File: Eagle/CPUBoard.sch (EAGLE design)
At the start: 32 parts, among them IC2 MAX232, IC3 MAX485CPA, J1 DISPLAY, J2 BUTTON_BOARD, J3 RELAY_BOARD, Q1 12.000MHz, X6 MKDSN1,5/3-5,08, X7 MKDSN1,5/3-5,08

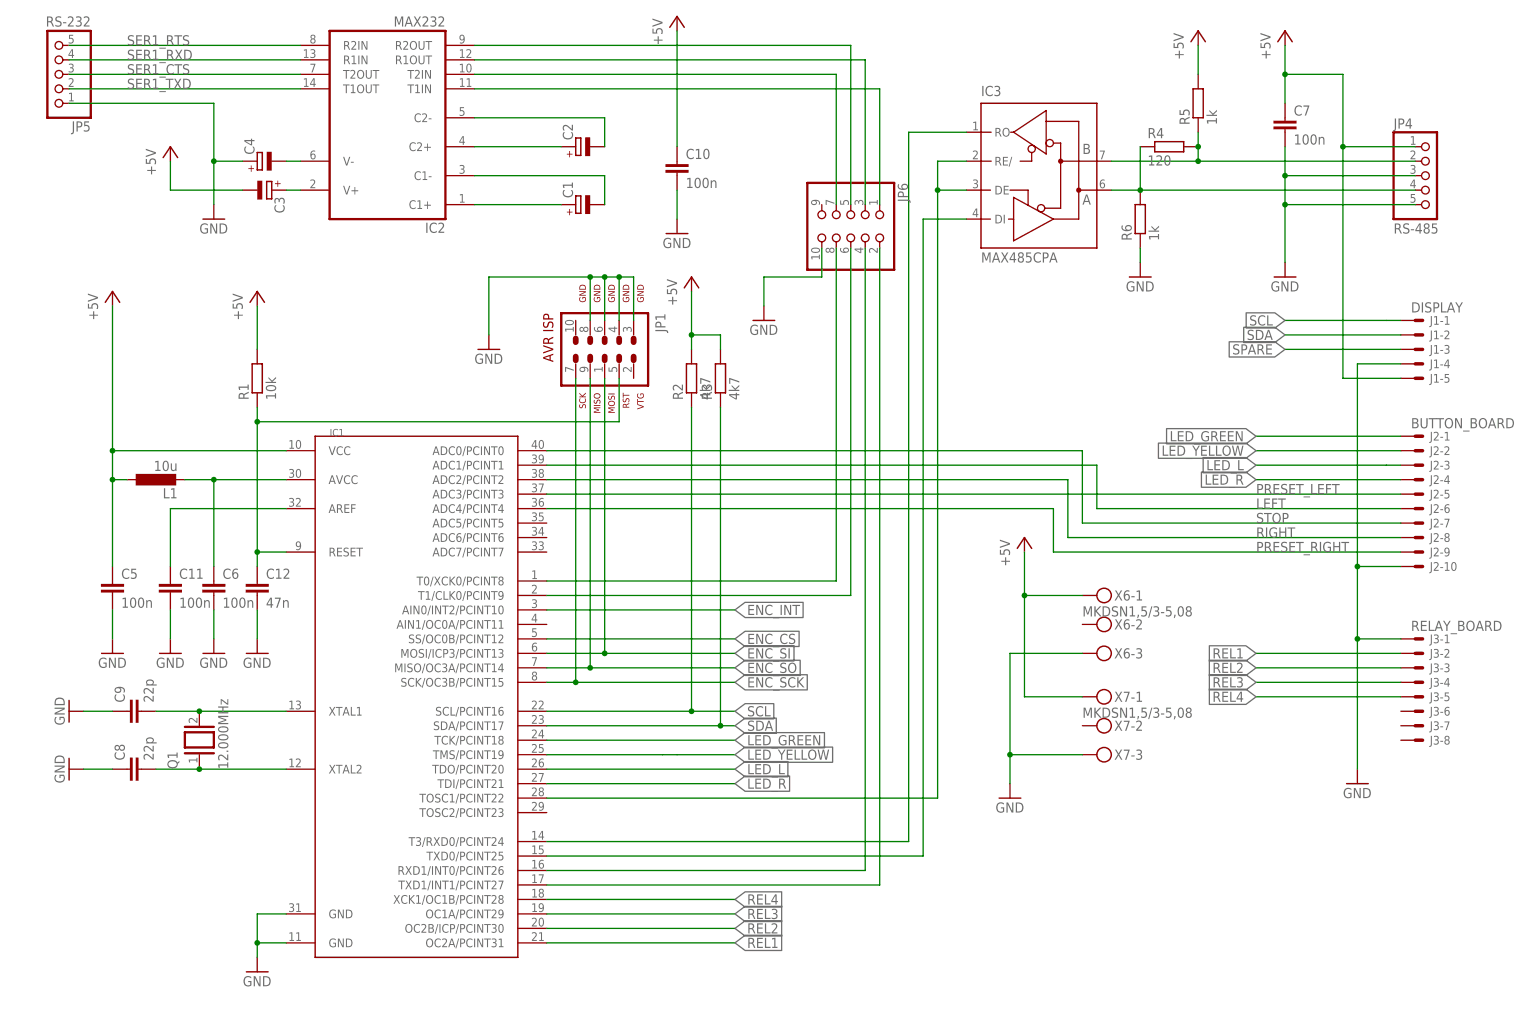
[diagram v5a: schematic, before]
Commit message: - corrections for RelayBoard1:   - using right connectors from library con-molex   - single sided routing - corrections for ButtonBoard:   - using right connector from library con-molex   - using right switches from library switch-misc (SRK/SRKL) - component placement & board layout for ButtonBoard done - CPUBoard:   - some components moved around the board   - re-routing (partially)
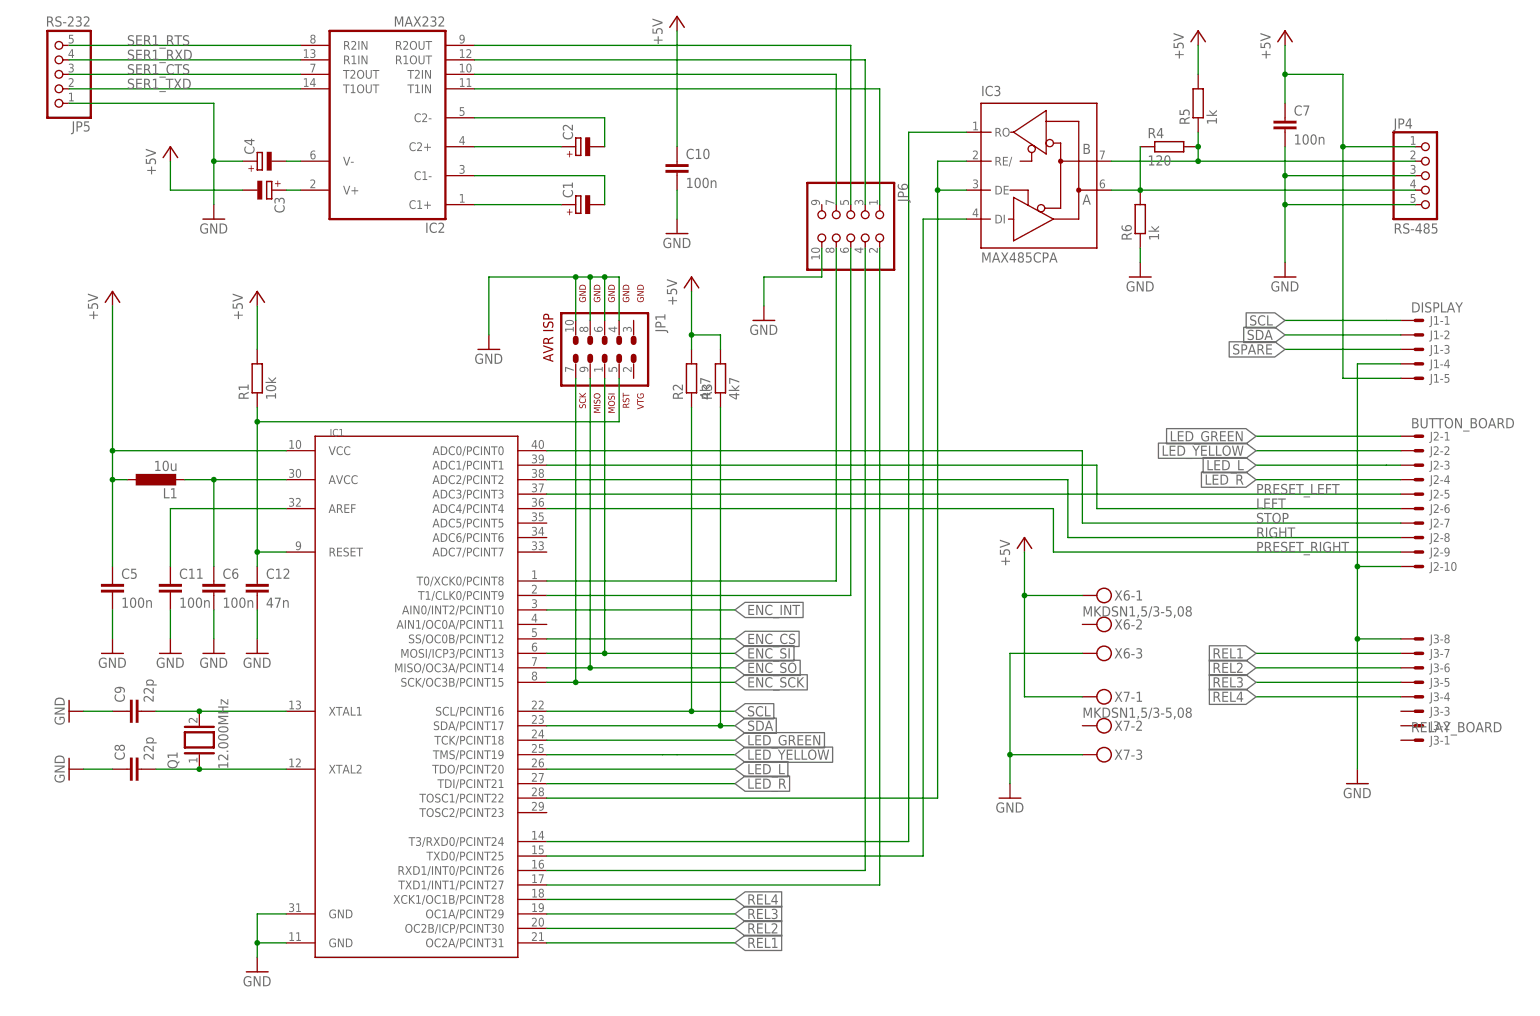
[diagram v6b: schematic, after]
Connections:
- net GND: now also J3-8.S, JP1.10; no longer J3-1.S, JP1.3
- net REL1: now also J3-7.S; no longer J3-2.S
- net REL2: now also J3-6.S; no longer J3-3.S
- net REL3: now also J3-5.S; no longer J3-4.S
- net REL4: now also J3-4.S; no longer J3-5.S
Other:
- moved on the sheet: J3-1, J3-2, J3-3, J3-4, J3-5, J3-6, J3-7, J3-8
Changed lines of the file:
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@@
 <instance part="J2" gate="-9" x="243.84" y="83.82"/>
 <instance part="J2" gate="-10" x="243.84" y="81.28"/>
-<instance part="J3" gate="-1" x="243.84" y="68.58"/>
-<instance part="J3" gate="-2" x="243.84" y="66.04"/>
-<instance part="J3" gate="-3" x="243.84" y="63.5"/>
-<instance part="J3" gate="-4" x="243.84" y="60.96"/>
-<instance part="J3" gate="-5" x="243.84" y="58.42"/>
-<instance part="J3" gate="-6" x="243.84" y="55.88"/>
-<instance part="J3" gate="-7" x="243.84" y="53.34"/>
-<instance part="J3" gate="-8" x="243.84" y="50.8"/>
+<instance part="J3" gate="-1" x="243.84" y="50.8"/>
+<instance part="J3" gate="-2" x="243.84" y="53.34"/>
+<instance part="J3" gate="-3" x="243.84" y="55.88"/>
+<instance part="J3" gate="-4" x="243.84" y="58.42"/>
+<instance part="J3" gate="-5" x="243.84" y="60.96"/>
+<instance part="J3" gate="-6" x="243.84" y="63.5"/>
+<instance part="J3" gate="-7" x="243.84" y="66.04"/>
+<instance part="J3" gate="-8" x="243.84" y="68.58"/>
 </instances>
 <busses>
@@
 </segment>
 <segment>
-<pinref part="JP1" gate="G$1" pin="3"/>
-<wire x1="106.68" y1="124.46" x2="106.68" y2="132.08" width="0.1524" layer="91"/>
-<wire x1="106.68" y1="132.08" x2="104.14" y2="132.08" width="0.1524" layer="91"/>
 <pinref part="GND10" gate="1" pin="GND"/>
 <wire x1="104.14" y1="132.08" x2="101.6" y2="132.08" width="0.1524" layer="91"/>
 <wire x1="101.6" y1="132.08" x2="99.06" y2="132.08" width="0.1524" layer="91"/>
-<wire x1="99.06" y1="132.08" x2="81.28" y2="132.08" width="0.1524" layer="91"/>
+<wire x1="99.06" y1="132.08" x2="96.52" y2="132.08" width="0.1524" layer="91"/>
+<wire x1="96.52" y1="132.08" x2="81.28" y2="132.08" width="0.1524" layer="91"/>
 <wire x1="81.28" y1="132.08" x2="81.28" y2="121.92" width="0.1524" layer="91"/>
 <pinref part="JP1" gate="G$1" pin="4"/>
 <wire x1="104.14" y1="124.46" x2="104.14" y2="132.08" width="0.1524" layer="91"/>
-<junction x="104.14" y="132.08"/>
 <pinref part="JP1" gate="G$1" pin="6"/>
 <wire x1="101.6" y1="124.46" x2="101.6" y2="132.08" width="0.1524" layer="91"/>
@@
 <wire x1="99.06" y1="124.46" x2="99.06" y2="132.08" width="0.1524" layer="91"/>
 <junction x="99.06" y="132.08"/>
+<pinref part="JP1" gate="G$1" pin="10"/>
+<wire x1="96.52" y1="124.46" x2="96.52" y2="132.08" width="0.1524" layer="91"/>
+<junction x="96.52" y="132.08"/>
 </segment>
 <segment>
 <pinref part="GND11" gate="1" pin="GND"/>
 <wire x1="233.68" y1="45.72" x2="233.68" y2="68.58" width="0.1524" layer="91"/>
-<wire x1="233.68" y1="68.58" x2="241.3" y2="68.58" width="0.1524" layer="91"/>
+<wire x1="233.68" y1="68.58" x2="233.68" y2="81.28" width="0.1524" layer="91"/>
 <wire x1="241.3" y1="81.28" x2="233.68" y2="81.28" width="0.1524" layer="91"/>
-<wire x1="233.68" y1="81.28" x2="233.68" y2="68.58" width="0.1524" layer="91"/>
-<junction x="233.68" y="68.58"/>
 <wire x1="233.68" y1="116.84" x2="233.68" y2="81.28" width="0.1524" layer="91"/>
 <junction x="233.68" y="81.28"/>
@@
 <pinref part="J1" gate="-4" pin="S"/>
 <pinref part="J2" gate="-10" pin="S"/>
-<pinref part="J3" gate="-1" pin="S"/>
+<pinref part="J3" gate="-8" pin="S"/>
+<wire x1="241.3" y1="68.58" x2="233.68" y2="68.58" width="0.1524" layer="91"/>
+<junction x="233.68" y="68.58"/>
 </segment>
 <segment>
@@
 <net name="REL1" class="0">
 <segment>
-<wire x1="241.3" y1="66.04" x2="215.9" y2="66.04" width="0.1524" layer="91"/>
 <label x="215.9" y="66.04" size="1.778" layer="95" rot="MR0" xref="yes"/>
-<pinref part="J3" gate="-2" pin="S"/>
+<pinref part="J3" gate="-7" pin="S"/>
+<wire x1="215.9" y1="66.04" x2="241.3" y2="66.04" width="0.1524" layer="91"/>
 </segment>
 <segment>
@@
 <net name="REL2" class="0">
 <segment>
+<label x="215.9" y="63.5" size="1.778" layer="95" rot="MR0" xref="yes"/>
+<pinref part="J3" gate="-6" pin="S"/>
 <wire x1="241.3" y1="63.5" x2="215.9" y2="63.5" width="0.1524" layer="91"/>
-<label x="215.9" y="63.5" size="1.778" layer="95" rot="MR0" xref="yes"/>
-<pinref part="J3" gate="-3" pin="S"/>
 </segment>
 <segment>
@@
 <net name="REL3" class="0">
 <segment>
-<wire x1="241.3" y1="60.96" x2="215.9" y2="60.96" width="0.1524" layer="91"/>
 <label x="215.9" y="60.96" size="1.778" layer="95" rot="MR0" xref="yes"/>
-<pinref part="J3" gate="-4" pin="S"/>
+<pinref part="J3" gate="-5" pin="S"/>
+<wire x1="215.9" y1="60.96" x2="241.3" y2="60.96" width="0.1524" layer="91"/>
 </segment>
 <segment>
@@
 <net name="REL4" class="0">
 <segment>
-<wire x1="241.3" y1="58.42" x2="215.9" y2="58.42" width="0.1524" layer="91"/>
 <label x="215.9" y="58.42" size="1.778" layer="95" rot="MR0" xref="yes"/>
-<pinref part="J3" gate="-5" pin="S"/>
-</segment>
-<segment>
+<pinref part="J3" gate="-4" pin="S"/>
+<wire x1="215.9" y1="58.42" x2="241.3" y2="58.42" width="0.1524" layer="91"/>
+</segment>
+<segment>

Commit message: - CPUBoard:   - another pin-header added for RS-485 UART   - correct termination for RS-485 A/B lines - PowerSupply: terminals added - eagle_clean.sh: remove backup files of Eagle
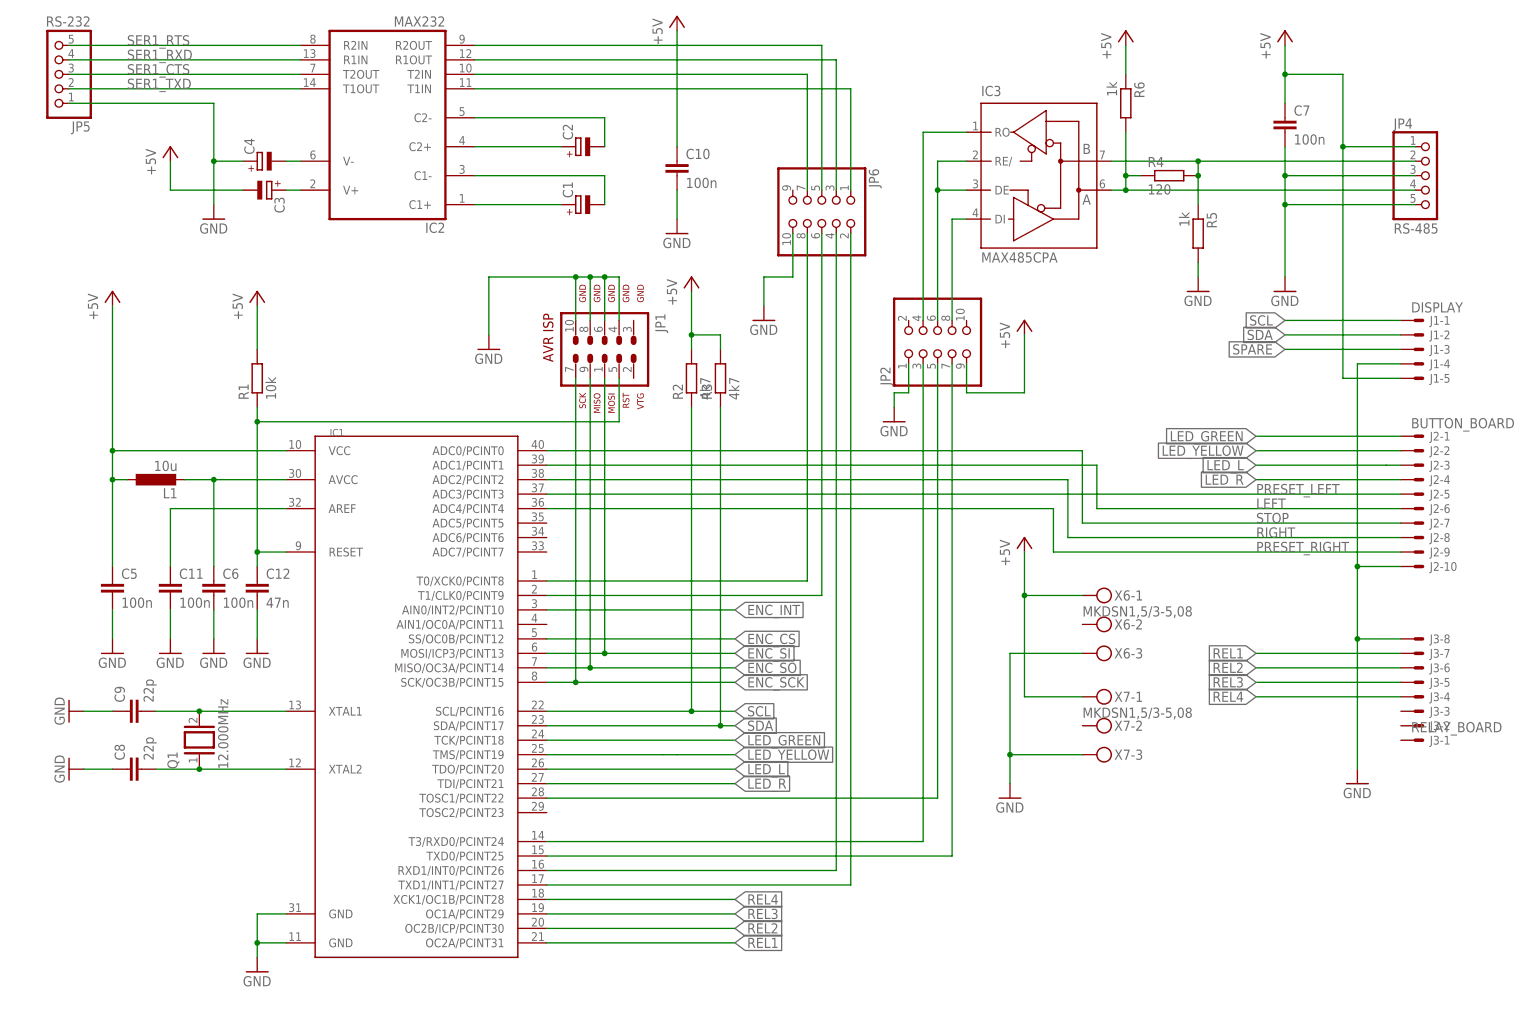
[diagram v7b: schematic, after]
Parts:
- added JP2: (no value), pinhead:PINHD-2X5
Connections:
- new net N$20: IC3G$1.DE, IC3G$1.RE/, JP2.6
- new net N$21: IC3G$1.DI, JP2.8
- new net N$23: IC3G$1.RO, JP2.4
- net +5V: now also JP2.9, R6.1; no longer R5.2
- net GND: now also JP2.1, R5.2; no longer R6.1
- net N$13: now also JP2.3; no longer IC3G$1.RO
- net N$14: now also JP2.7; no longer IC3G$1.DI
- net N$15: now also JP2.5; no longer IC3G$1.DE, IC3G$1.RE/
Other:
- moved on the sheet: JP6, R4, R5, R6

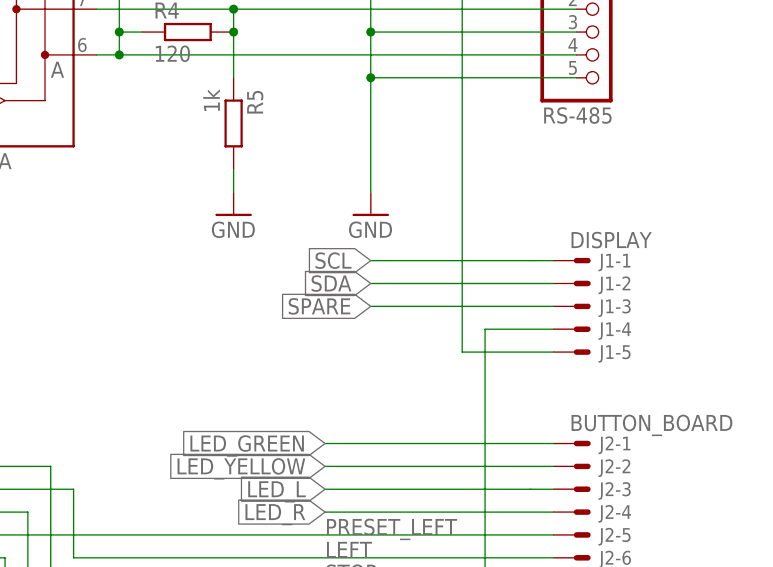
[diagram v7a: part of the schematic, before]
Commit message: - CPUBoard: fix connections to display, somehow mirrored
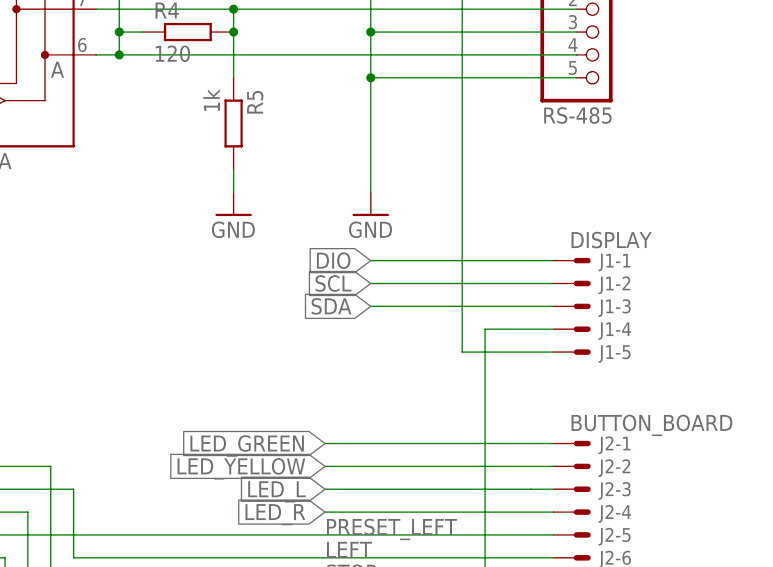
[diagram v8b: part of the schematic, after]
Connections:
- removed net SPARE: J1-3.S
- new net DIO: J1-1.S
- net SCL: now also J1-2.S; no longer J1-1.S
- net SDA: now also J1-3.S; no longer J1-2.S
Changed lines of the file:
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@@
-</segment>
-</net>
-<net name="SPARE" class="0">
-<segment>
-<wire x1="241.3" y1="119.38" x2="220.98" y2="119.38" width="0.1524" layer="91"/>
-<label x="220.98" y="119.38" size="1.778" layer="95" rot="MR0" xref="yes"/>
-<pinref part="J1" gate="-3" pin="S"/>
 </segment>
 </net>
@@
 </segment>
 <segment>
-<wire x1="241.3" y1="124.46" x2="238.76" y2="124.46" width="0.1524" layer="91"/>
-<label x="220.98" y="124.46" size="1.778" layer="95" rot="MR0" xref="yes"/>
-<pinref part="J1" gate="-1" pin="S"/>
-<wire x1="238.76" y1="124.46" x2="220.98" y2="124.46" width="0.1524" layer="91"/>
+<label x="220.98" y="121.92" size="1.778" layer="95" rot="MR0" xref="yes"/>
+<wire x1="241.3" y1="121.92" x2="220.98" y2="121.92" width="0.1524" layer="91"/>
+<pinref part="J1" gate="-2" pin="S"/>
 </segment>
 </net>
@@
 </segment>
 <segment>
-<wire x1="241.3" y1="121.92" x2="220.98" y2="121.92" width="0.1524" layer="91"/>
-<label x="220.98" y="121.92" size="1.778" layer="95" rot="MR0" xref="yes"/>
-<pinref part="J1" gate="-2" pin="S"/>
+<label x="220.98" y="119.38" size="1.778" layer="95" rot="MR0" xref="yes"/>
+<wire x1="241.3" y1="119.38" x2="220.98" y2="119.38" width="0.1524" layer="91"/>
+<pinref part="J1" gate="-3" pin="S"/>
 </segment>
 </net>
@@
 </segment>
 </net>
+<net name="DIO" class="0">
+<segment>
+<label x="220.98" y="124.46" size="1.778" layer="95" rot="MR0" xref="yes"/>
+<wire x1="220.98" y1="124.46" x2="241.3" y2="124.46" width="0.1524" layer="91"/>
+<pinref part="J1" gate="-1" pin="S"/>
+</segment>
+</net>
